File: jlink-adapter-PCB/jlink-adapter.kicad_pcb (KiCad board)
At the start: 4 copper layers, 25.5 x 27 mm, 14 parts, among them J1 Conn_02x10_Odd_Even, J2 Conn_02x05_Odd_Even, J3 Tag-Connect IDC, Q1 BSS123TA

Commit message: Remove possible issue component to clear up KiCAD DRC
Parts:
- removed REF**: layer-label-4, SKEC_Footprints:layer-label-4-(F_B)
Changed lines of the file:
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@@
 	(net 23 "Net-(JP1-A)")
 	(net 24 "Net-(JP2-A)")
-	(footprint "SKEC_Footprints:layer-label-4-(F_B)"
-		(layer "F.Cu")
-		(at 60.72 52.8)
-		(descr "Text indicators for copper layers")
-		(property "Reference" "REF**"
-			(at 0 2 0)
-			(unlocked yes)
-			(layer "F.SilkS")
-			(hide yes)
-			(effects
-				(font
-					(size 1 1)
-					(thickness 0.1)
-				)
-			)
-		)
-		(property "Value" "layer-label-4"
-			(at 0 1 0)
-			(unlocked yes)
-			(layer "F.Fab")
-			(hide yes)
-			(effects
-				(font
-					(size 1 1)
-					(thickness 0.15)
-				)
-			)
-		)
-		(property "Footprint" "SKEC_Footprints:layer-label-4-(F_B)"
-			(at 0 0 0)
-			(unlocked yes)
-			(layer "F.Fab")
-			(hide yes)
-			(effects
-				(font
-					(size 1 1)
-					(thickness 0.15)
-				)
-			)
-		)
-		(property "Datasheet" ""
-			(at 0 0 0)
-			(unlocked yes)
-			(layer "F.Fab")
-			(hide yes)
-			(effects
-				(font
-					(size 1 1)
-					(thickness 0.15)
-				)
-			)
-		)
-		(property "Description" ""
-			(at 0 0 0)
-			(unlocked yes)
-			(layer "F.Fab")
-			(hide yes)
-			(effects
-				(font
-					(size 1 1)
-					(thickness 0.15)
-				)
-			)
-		)
-		(attr board_only exclude_from_pos_files exclude_from_bom)
-		(fp_text user "F"
-			(at 0 -0.2 0)
-			(unlocked yes)
-			(layer "F.Cu")
-			(effects
-				(font
-					(size 1 1)
-					(thickness 0.125)
-				)
-				(justify left bottom)
-			)
-		)
-		(fp_text user "2"
-			(at 1 -0.2 0)
-			(unlocked yes)
-			(layer "In1.Cu")
-			(effects
-				(font
-					(size 1 1)
-					(thickness 0.125)
-				)
-				(justify left bottom)
-			)
-		)
-		(fp_text user "3"
-			(at 2 -0.2 0)
-			(unlocked yes)
-			(layer "In2.Cu")
-			(effects
-				(font
-					(size 1 1)
-					(thickness 0.125)
-				)
-				(justify left bottom)
-			)
-		)
-		(fp_text user "B"
-			(at 3 -0.2 0)
-			(unlocked yes)
-			(layer "B.Cu")
-			(effects
-				(font
-					(size 1 1)
-					(thickness 0.125)
-				)
-				(justify left bottom)
-			)
-		)
-		(zone
-			(net 0)
-			(net_name "")
-			(layers "*.Cu")
-			(hatch edge 0.5)
-			(connect_pads
-				(clearance 0)
-			)
-			(min_thickness 0.25)
-			(filled_areas_thickness no)
-			(keepout
-				(tracks not_allowed)
-				(vias not_allowed)
-				(pads not_allowed)
-				(copperpour not_allowed)
-				(footprints allowed)
-			)
-			(fill
-				(thermal_gap 0.5)
-				(thermal_bridge_width 0.5)
-			)
-			(polygon
-				(pts
-					(xy 60.72 52.8) (xy 60.72 51.2) (xy 64.72 51.2) (xy 64.72 52.8)
-				)
-			)
-		)
-	)
 	(footprint "LED_SMD:LED_1206_3216Metric_Pad1.42x1.75mm_HandSolder"
 		(layer "F.Cu")

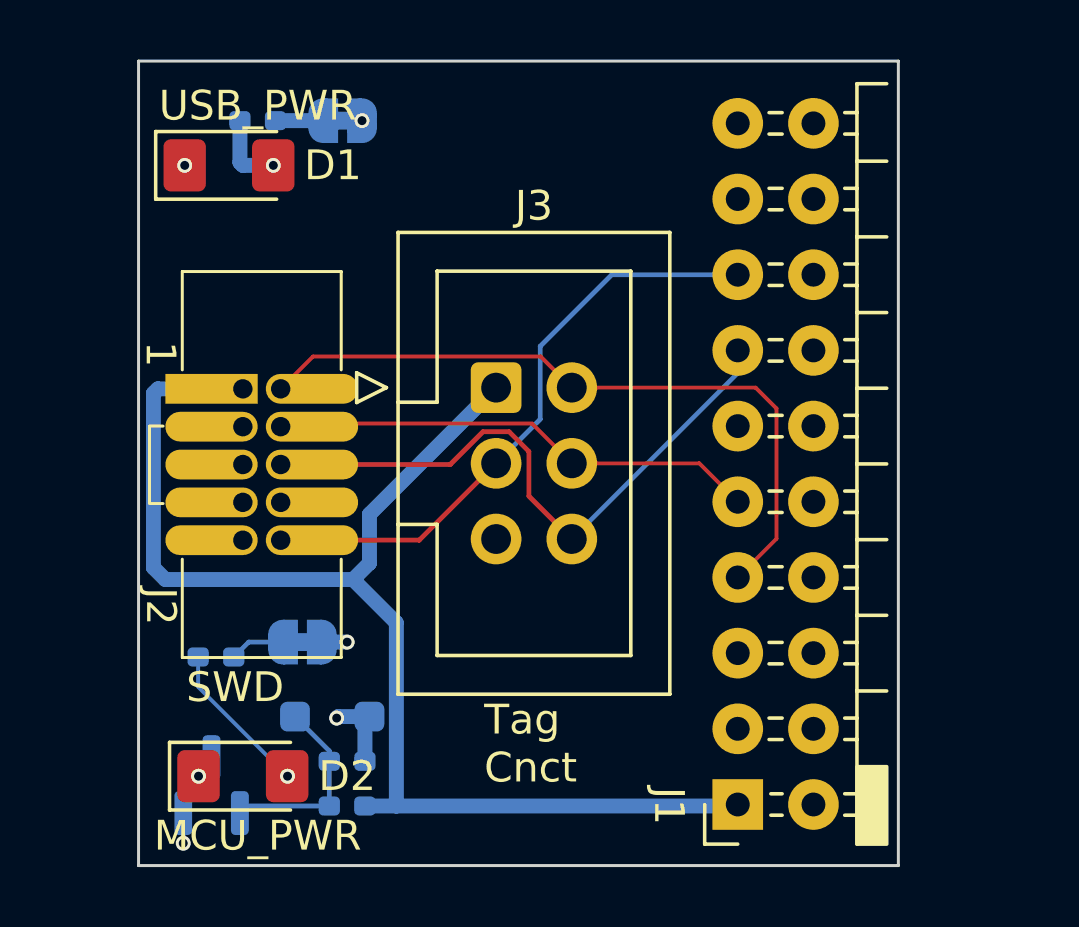
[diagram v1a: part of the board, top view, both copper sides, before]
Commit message: Add features and minor improvements from V4
* Add Custom Segger Adapter
* Add a 5V tap off point
* Add a reset button for the MCU
* Remove Jumpers
* Swapped the Inner Plane to supply Vtref, rather than 5V, as 5V goes to fewer places.
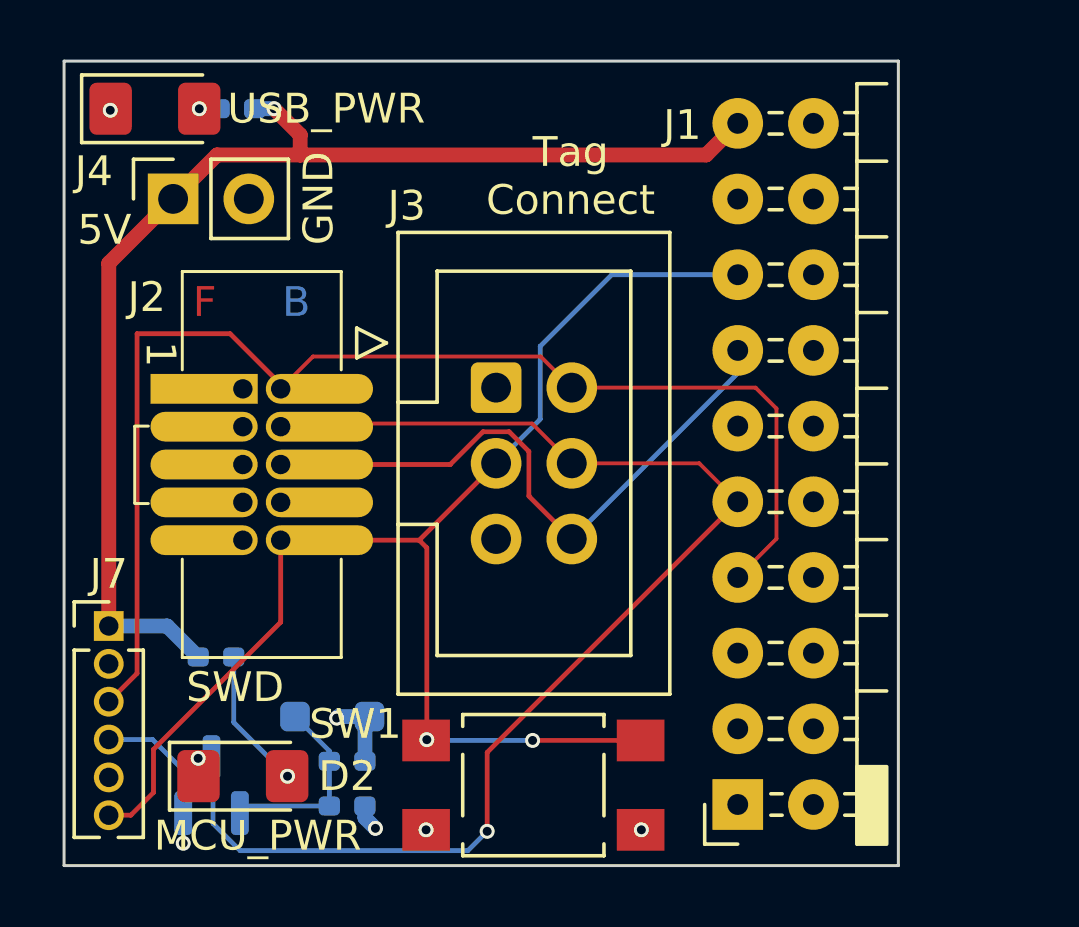
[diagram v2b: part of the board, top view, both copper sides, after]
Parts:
- removed JP1, JP2: Jumper_2_Bridged, Jumper:SolderJumper-2_P1.3mm_Bridged_RoundedPad1.0x1.5mm
- added J4: Conn_01x02, Connector_PinSocket_2.54mm:PinSocket_1x02_P2.54mm_Vertical, F.Cu at (51.2, 54.6)
- added J7: Custom Segger Adapter, Connector_PinHeader_1.27mm:PinHeader_1x06_P1.27mm_Vertical, F.Cu at (49.0, 69.0)
- added REF**: layer-label-4, SKEC_Footprints:layer-label-4-(F_B), F.Cu at (51.8, 58.9)
- added SW1: SW_Push, Button_Switch_SMD:SW_SPST_TL3305B, F.Cu at (63.2, 74.3)
- R3: value 100 -> 1k
- moved D1 3.13 mm to (50.5, 51.6)
- moved R1 0.81 mm to (53.3, 51.6)
- turned R2 to 0 degrees
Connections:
- R1 pad 1: Net-(JP1-A) -> +5V
- R2 pad 1: Net-(JP2-A) -> +5V
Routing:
- net /VTREF: track 44.9 -> 1.17 mm, vias 0 -> 1
- net +5V: track 0.87 -> 41.2 mm, vias 2 -> 1
- net /SWCLK: track 16.5 -> 46.0 mm, vias 0 -> 1
- net /RESET: track 22.4 -> 48.5 mm, vias 0 -> 2
- net /SWDIO: track 24.0 -> 42.4 mm
- net Net-(D1-A): track 2.56 -> 0.66 mm
- net Net-(JP2-A): track 1.86 -> 0.00 mm
- net Net-(JP1-A): track 1.60 -> 0.00 mm
- net GND: track 3.93 -> 3.96 mm, vias 3 -> 5
- added copper zone on In2.Cu, net /VTREF
- removed copper zone on In2.Cu, net +5V
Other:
- board size 25.5 x 27 mm -> 28 x 27 mm
- board text added: "5V"
- board text added: "GND"
- board text added: "SKEC V4"
- board text added: "Tag Connect"
- board text removed: "SKEC V3"
- board text removed: "Tag Cnct"
